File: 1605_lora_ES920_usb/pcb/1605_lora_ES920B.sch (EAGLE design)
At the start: 24 parts, among them IC1 FT231XQ, U2 ES920LR_MODULE

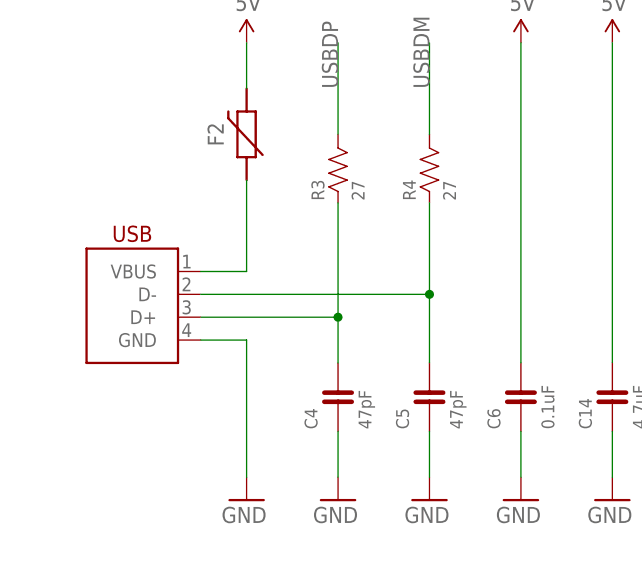
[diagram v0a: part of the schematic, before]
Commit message: Add lora module.
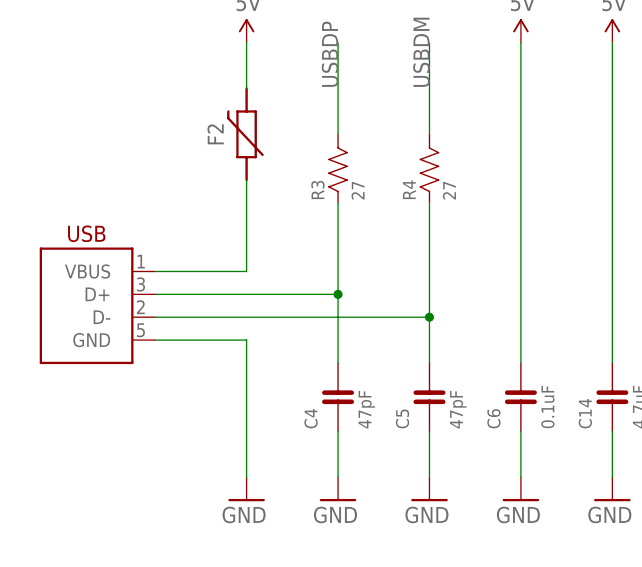
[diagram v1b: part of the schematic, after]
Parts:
- USB1: device FaBo-USB:USB-B_PTH -> FaBo-USB:USB-MICRO_B_SMT_HIROSE
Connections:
- new net N$1: RESET.3, RESET.4
- net GND: no longer RESET.3, RESET.4
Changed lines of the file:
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@@
 <part name="R7" library="FaBo-Resistors" deviceset="RESISTOR" device="-0603-NARROW" value="1k"/>
 <part name="GND24" library="FaBo-Supply" deviceset="GND" device=""/>
-<part name="USB1" library="FaBo-USB" deviceset="USB" device="-B_PTH"/>
 <part name="GND3" library="FaBo-Supply" deviceset="GND" device=""/>
 <part name="GND9" library="FaBo-Supply" deviceset="GND" device=""/>
@@
 <part name="U$2" library="FaBo-Logo" deviceset="LOGO_OSHW" device="-M_BOTTOM"/>
 <part name="U2" library="FaBo-LoRa" deviceset="ES920LR_MODULE" device=""/>
+<part name="USB1" library="FaBo-USB" deviceset="USB" device="-MICRO_B_SMT_HIROSE"/>
 </parts>
 <sheets>
@@
 <attribute name="VALUE" x="172.466" y="111.76" size="1.778" layer="96"/>
 </instance>
-<instance part="USB1" gate="G$1" x="20.32" y="127" smashed="yes"/>
 <instance part="GND3" gate="G$1" x="134.62" y="96.52" smashed="yes">
 <attribute name="VALUE" x="131.826" y="91.44" size="1.778" layer="96"/>
@@
 <instance part="U$2" gate="G$1" x="248.92" y="12.7" smashed="yes"/>
 <instance part="U2" gate="G$1" x="170.18" y="73.66" smashed="yes"/>
+<instance part="USB1" gate="G$1" x="15.24" y="127" smashed="yes"/>
 </instances>
 <busses>
@@
 <nets>
 <net name="GND" class="0">
-<segment>
-<pinref part="GND15" gate="G$1" pin="GND"/>
-<wire x1="40.64" y1="38.1" x2="40.64" y2="17.78" width="0.1524" layer="91"/>
-<pinref part="RESET" gate="G$1" pin="3"/>
-<wire x1="35.56" y1="40.64" x2="40.64" y2="40.64" width="0.1524" layer="91"/>
-<wire x1="40.64" y1="40.64" x2="40.64" y2="38.1" width="0.1524" layer="91"/>
-<pinref part="RESET" gate="G$1" pin="4"/>
-<wire x1="35.56" y1="38.1" x2="40.64" y2="38.1" width="0.1524" layer="91"/>
-</segment>
 <segment>
 <pinref part="GND1" gate="G$1" pin="GND"/>
@@
 <segment>
 <pinref part="GND7" gate="G$1" pin="GND"/>
-<wire x1="27.94" y1="124.46" x2="33.02" y2="124.46" width="0.1524" layer="91"/>
+<wire x1="22.86" y1="124.46" x2="33.02" y2="124.46" width="0.1524" layer="91"/>
 <wire x1="33.02" y1="124.46" x2="33.02" y2="109.22" width="0.1524" layer="91"/>
 <pinref part="USB1" gate="G$1" pin="GND"/>
@@
 <segment>
 <wire x1="40.64" y1="40.64" x2="35.56" y2="40.64" width="0.1524" layer="91"/>
+<pinref part="GND15" gate="G$1" pin="GND"/>
+<wire x1="40.64" y1="38.1" x2="40.64" y2="17.78" width="0.1524" layer="91"/>
+<pinref part="RESET" gate="G$1" pin="3"/>
+<wire x1="35.56" y1="40.64" x2="40.64" y2="40.64" width="0.1524" layer="91"/>
+<wire x1="40.64" y1="40.64" x2="40.64" y2="38.1" width="0.1524" layer="91"/>
+<pinref part="RESET" gate="G$1" pin="4"/>
+<wire x1="35.56" y1="38.1" x2="40.64" y2="38.1" width="0.1524" layer="91"/>
 </segment>
 </net>
@@
 <net name="N$7" class="0">
 <segment>
-<wire x1="53.34" y1="129.54" x2="27.94" y2="129.54" width="0.1524" layer="91"/>
-<wire x1="53.34" y1="121.92" x2="53.34" y2="129.54" width="0.1524" layer="91"/>
-<wire x1="53.34" y1="139.7" x2="53.34" y2="129.54" width="0.1524" layer="91"/>
-<junction x="53.34" y="129.54"/>
+<wire x1="53.34" y1="127" x2="22.86" y2="127" width="0.1524" layer="91"/>
+<wire x1="53.34" y1="121.92" x2="53.34" y2="127" width="0.1524" layer="91"/>
+<wire x1="53.34" y1="139.7" x2="53.34" y2="127" width="0.1524" layer="91"/>
+<junction x="53.34" y="127"/>
 <pinref part="R4" gate="G$1" pin="1"/>
 <pinref part="C5" gate="G$1" pin="2"/>
@@
 <net name="N$8" class="0">
 <segment>
-<wire x1="43.18" y1="139.7" x2="43.18" y2="127" width="0.1524" layer="91"/>
-<wire x1="43.18" y1="127" x2="27.94" y2="127" width="0.1524" layer="91"/>
-<wire x1="43.18" y1="121.92" x2="43.18" y2="127" width="0.1524" layer="91"/>
-<junction x="43.18" y="127"/>
+<wire x1="43.18" y1="139.7" x2="43.18" y2="129.54" width="0.1524" layer="91"/>
+<wire x1="43.18" y1="129.54" x2="22.86" y2="129.54" width="0.1524" layer="91"/>
+<wire x1="43.18" y1="121.92" x2="43.18" y2="129.54" width="0.1524" layer="91"/>
+<junction x="43.18" y="129.54"/>
 <pinref part="R3" gate="G$1" pin="1"/>
 <pinref part="C4" gate="G$1" pin="2"/>
@@
 <net name="VBUS1" class="0">
 <segment>
-<wire x1="27.94" y1="132.08" x2="33.02" y2="132.08" width="0.1524" layer="91"/>
+<wire x1="22.86" y1="132.08" x2="33.02" y2="132.08" width="0.1524" layer="91"/>
 <wire x1="33.02" y1="132.08" x2="33.02" y2="142.24" width="0.1524" layer="91"/>
 <pinref part="F2" gate="G$1" pin="1"/>
